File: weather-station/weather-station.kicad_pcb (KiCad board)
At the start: 2 copper layers, 62 x 100 mm, 23 parts, among them P1 CONN_01X05, P2 CONN_01X03, P3 CONN_01X02, P8 CONN_RB, U1 FUELGUAGE, U2 FEATHER, U3 pololu-vreg, U4 adafruit-solar-charger, U5 FEATHER

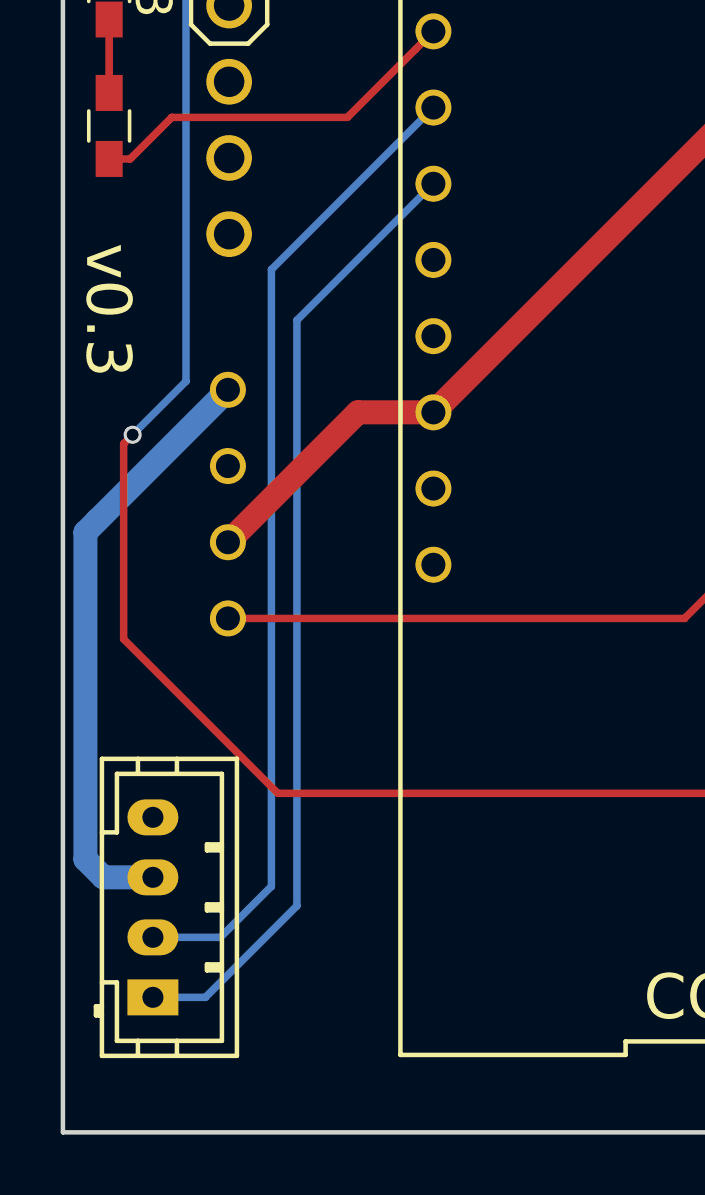
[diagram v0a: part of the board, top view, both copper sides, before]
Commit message: Change RB connector footprint to 2.54mm pitch.
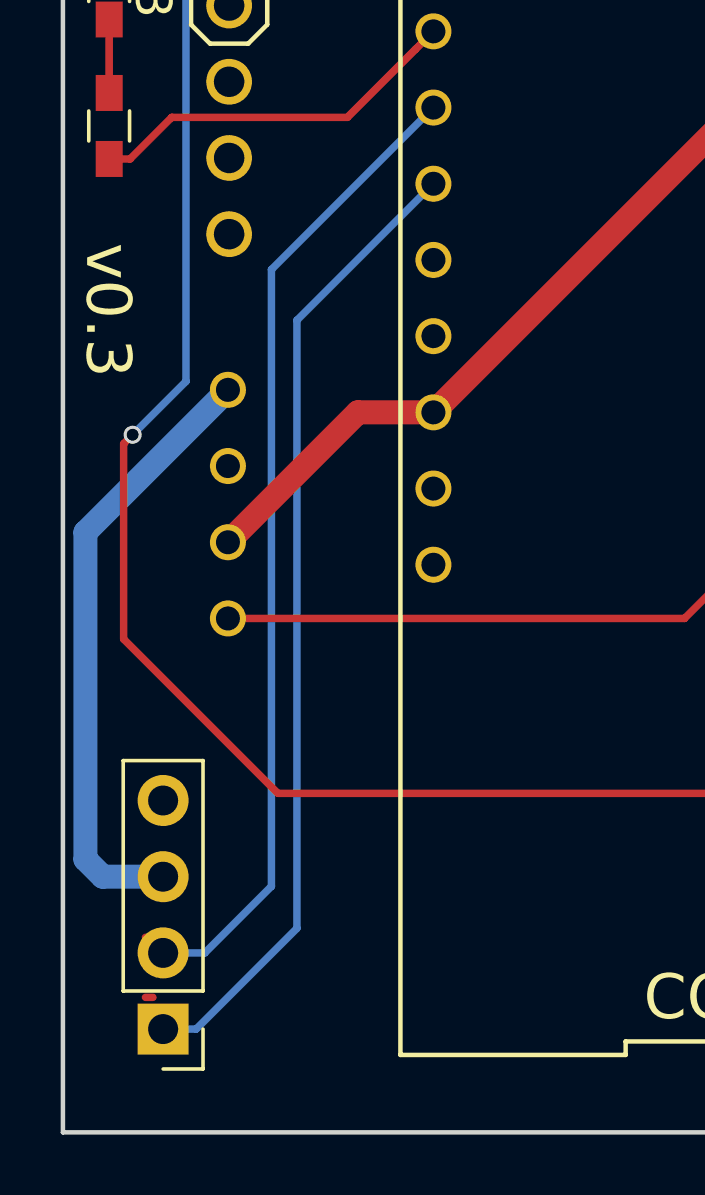
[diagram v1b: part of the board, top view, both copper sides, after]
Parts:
- P8: footprint Connectors_JST:JST_PH_B4B-PH-K_04x2.00mm_Straight -> Socket_Strips:Socket_Strip_Straight_1x04_Pitch2.54mm
- moved P8 1.11 mm to (53.3, 146.6), turned to 180 degrees
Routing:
- net (no net): track 0.00 -> 0.50 mm
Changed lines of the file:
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@@
   (general
     (links 55)
-    (no_connects 0)
+    (no_connects 16)
     (area 49.924999 49.924999 112.075001 150.075001)
     (thickness 1.6)
     (drawings 17)
-    (tracks 192)
+    (tracks 190)
     (zones 0)
     (modules 23)
@@
   )
   (setup
-    (last_trace_width 0.25)
+    (last_trace_width 0.8)
     (user_trace_width 0.203)
     (user_trace_width 0.4)
@@
       (xy -6.476371 1.79874)) (layer B.SilkS) (width 0.01))
   )
-  (module Connectors_JST:JST_PH_B4B-PH-K_04x2.00mm_Straight (layer F.Cu)
-    (at 53 145.5 90)
-    (descr http://www.jst-mfg.com/product/pdf/eng/ePH.pdf)
-    (tags "connector jst ph")
-    (fp_text reference P8 (at -1.5 4 90) (layer F.SilkS) hide
-      (effects (font (size 1 1) (thickness 0.15)))
-    )
-    (fp_text value CONN_RB (at 3 4 90) (layer F.Fab) hide
-      (effects (font (size 1 1) (thickness 0.15)))
-    )
-    (fp_line (start -1.95 2.8) (end -1.95 -1.7) (layer F.SilkS) (width 0.15))
-    (fp_line (start -1.95 -1.7) (end 7.95 -1.7) (layer F.SilkS) (width 0.15))
-    (fp_line (start 7.95 -1.7) (end 7.95 2.8) (layer F.SilkS) (width 0.15))
-    (fp_line (start 7.95 2.8) (end -1.95 2.8) (layer F.SilkS) (width 0.15))
-    (fp_line (start 0.5 -1.7) (end 0.5 -1.2) (layer F.SilkS) (width 0.15))
-    (fp_line (start 0.5 -1.2) (end -1.45 -1.2) (layer F.SilkS) (width 0.15))
-    (fp_line (start -1.45 -1.2) (end -1.45 2.3) (layer F.SilkS) (width 0.15))
-    (fp_line (start -1.45 2.3) (end 7.45 2.3) (layer F.SilkS) (width 0.15))
-    (fp_line (start 7.45 2.3) (end 7.45 -1.2) (layer F.SilkS) (width 0.15))
-    (fp_line (start 7.45 -1.2) (end 5.5 -1.2) (layer F.SilkS) (width 0.15))
-    (fp_line (start 5.5 -1.2) (end 5.5 -1.7) (layer F.SilkS) (width 0.15))
-    (fp_line (start -1.95 -0.5) (end -1.45 -0.5) (layer F.SilkS) (width 0.15))
-    (fp_line (start -1.95 0.8) (end -1.45 0.8) (layer F.SilkS) (width 0.15))
-    (fp_line (start 7.45 -0.5) (end 7.95 -0.5) (layer F.SilkS) (width 0.15))
-    (fp_line (start 7.45 0.8) (end 7.95 0.8) (layer F.SilkS) (width 0.15))
-    (fp_line (start -0.3 -1.7) (end -0.3 -1.9) (layer F.SilkS) (width 0.15))
-    (fp_line (start -0.3 -1.9) (end -0.6 -1.9) (layer F.SilkS) (width 0.15))
-    (fp_line (start -0.6 -1.9) (end -0.6 -1.7) (layer F.SilkS) (width 0.15))
-    (fp_line (start -0.3 -1.8) (end -0.6 -1.8) (layer F.SilkS) (width 0.15))
-    (fp_line (start 0.9 2.3) (end 0.9 1.8) (layer F.SilkS) (width 0.15))
-    (fp_line (start 0.9 1.8) (end 1.1 1.8) (layer F.SilkS) (width 0.15))
-    (fp_line (start 1.1 1.8) (end 1.1 2.3) (layer F.SilkS) (width 0.15))
-    (fp_line (start 1 2.3) (end 1 1.8) (layer F.SilkS) (width 0.15))
-    (fp_line (start 2.9 2.3) (end 2.9 1.8) (layer F.SilkS) (width 0.15))
-    (fp_line (start 2.9 1.8) (end 3.1 1.8) (layer F.SilkS) (width 0.15))
-    (fp_line (start 3.1 1.8) (end 3.1 2.3) (layer F.SilkS) (width 0.15))
-    (fp_line (start 3 2.3) (end 3 1.8) (layer F.SilkS) (width 0.15))
-    (fp_line (start 4.9 2.3) (end 4.9 1.8) (layer F.SilkS) (width 0.15))
-    (fp_line (start 4.9 1.8) (end 5.1 1.8) (layer F.SilkS) (width 0.15))
-    (fp_line (start 5.1 1.8) (end 5.1 2.3) (layer F.SilkS) (width 0.15))
-    (fp_line (start 5 2.3) (end 5 1.8) (layer F.SilkS) (width 0.15))
-    (fp_line (start -2.45 3.3) (end -2.45 -2.2) (layer F.CrtYd) (width 0.05))
-    (fp_line (start -2.45 -2.2) (end 8.45 -2.2) (layer F.CrtYd) (width 0.05))
-    (fp_line (start 8.45 -2.2) (end 8.45 3.3) (layer F.CrtYd) (width 0.05))
-    (fp_line (start 8.45 3.3) (end -2.45 3.3) (layer F.CrtYd) (width 0.05))
-    (pad 1 thru_hole rect (at 0 0 90) (size 1.2 1.7) (drill 0.7) (layers *.Cu *.Mask)
-      (net 10 /RB_RX))
-    (pad 2 thru_hole oval (at 2 0 90) (size 1.2 1.7) (drill 0.7) (layers *.Cu *.Mask)
-      (net 11 /RB_TX))
-    (pad 3 thru_hole oval (at 4 0 90) (size 1.2 1.7) (drill 0.7) (layers *.Cu *.Mask)
-      (net 5 +5V))
-    (pad 4 thru_hole oval (at 6 0 90) (size 1.2 1.7) (drill 0.7) (layers *.Cu *.Mask)
-      (net 3 GND))
-  )
   (module conservify:feather (layer F.Cu)
     (at 72.51 122.19 90)
@@
     )
   )
+  (module Socket_Strips:Socket_Strip_Straight_1x04_Pitch2.54mm (layer F.Cu)
+    (at 53.34 146.558 180)
+    (descr "Through hole straight socket strip, 1x04, 2.54mm pitch, single row")
+    (tags "Through hole socket strip THT 1x04 2.54mm single row")
+    (fp_text reference P8 (at 0 -2.33 180) (layer F.SilkS) hide
+      (effects (font (size 1 1) (thickness 0.15)))
+    )
+    (fp_text value CONN_RB (at 0 9.95 180) (layer F.Fab)
+      (effects (font (size 1 1) (thickness 0.15)))
+    )
+    (fp_line (start -1.27 -1.27) (end -1.27 8.89) (layer F.Fab) (width 0.1))
+    (fp_line (start -1.27 8.89) (end 1.27 8.89) (layer F.Fab) (width 0.1))
+    (fp_line (start 1.27 8.89) (end 1.27 -1.27) (layer F.Fab) (width 0.1))
+    (fp_line (start 1.27 -1.27) (end -1.27 -1.27) (layer F.Fab) (width 0.1))
+    (fp_line (start -1.33 1.27) (end -1.33 8.95) (layer F.SilkS) (width 0.12))
+    (fp_line (start -1.33 8.95) (end 1.33 8.95) (layer F.SilkS) (width 0.12))
+    (fp_line (start 1.33 8.95) (end 1.33 1.27) (layer F.SilkS) (width 0.12))
+    (fp_line (start 1.33 1.27) (end -1.33 1.27) (layer F.SilkS) (width 0.12))
+    (fp_line (start -1.33 0) (end -1.33 -1.33) (layer F.SilkS) (width 0.12))
+    (fp_line (start -1.33 -1.33) (end 0 -1.33) (layer F.SilkS) (width 0.12))
+    (fp_line (start -1.8 -1.8) (end -1.8 9.4) (layer F.CrtYd) (width 0.05))
+    (fp_line (start -1.8 9.4) (end 1.8 9.4) (layer F.CrtYd) (width 0.05))
+    (fp_line (start 1.8 9.4) (end 1.8 -1.8) (layer F.CrtYd) (width 0.05))
+    (fp_line (start 1.8 -1.8) (end -1.8 -1.8) (layer F.CrtYd) (width 0.05))
+    (fp_text user %R (at 0 -2.33 180) (layer F.Fab)
+      (effects (font (size 1 1) (thickness 0.15)))
+    )
+    (pad 1 thru_hole rect (at 0 0 180) (size 1.7 1.7) (drill 1) (layers *.Cu *.Mask)
+      (net 10 /RB_RX))
+    (pad 2 thru_hole oval (at 0 2.54 180) (size 1.7 1.7) (drill 1) (layers *.Cu *.Mask)
+      (net 11 /RB_TX))
+    (pad 3 thru_hole oval (at 0 5.08 180) (size 1.7 1.7) (drill 1) (layers *.Cu *.Mask)
+      (net 5 +5V))
+    (pad 4 thru_hole oval (at 0 7.62 180) (size 1.7 1.7) (drill 1) (layers *.Cu *.Mask)
+      (net 3 GND))
+    (model ${KISYS3DMOD}/Socket_Strips.3dshapes/Socket_Strip_Straight_1x04_Pitch2.54mm.wrl
+      (at (xyz 0 -0.15 0))
+      (scale (xyz 1 1 1))
+      (rotate (xyz 0 0 270))
+    )
+  )
   (gr_text D3 (at 53 111.7 270) (layer F.SilkS)
     (effects (font (size 1.2 1.2) (thickness 0.2)))
@@
   (gr_line (start 50 150) (end 112 150) (angle 90) (layer Edge.Cuts) (width 0.15))
   (gr_line (start 50 50) (end 50 150) (angle 90) (layer Edge.Cuts) (width 0.15))
+  (segment (start 53 143.5) (end 52.75 143.5) (width 0.25) (layer F.Cu) (net 0))
+  (segment (start 53 145.5) (end 52.75 145.5) (width 0.25) (layer F.Cu) (net 0))
   (segment (start 54.54 62.38) (end 54.54 58.06) (width 0.8) (layer F.Cu) (net 1))
   (segment (start 54.54 58.06) (end 58.1 54.5) (width 0.8) (layer F.Cu) (net 1))
@@
   (segment (start 85.75 122.92) (end 85.75 103.861998) (width 0.8) (layer B.Cu) (net 4))
   (segment (start 88.84 126.01) (end 85.75 122.92) (width 0.8) (layer B.Cu) (net 4))
-  (segment (start 50.75 140.9) (end 50.75 130) (width 0.8) (layer B.Cu) (net 5))
-  (segment (start 50.75 130) (end 51.14999 129.60001) (width 0.8) (layer B.Cu) (net 5))
-  (segment (start 53 141.5) (end 51.35 141.5) (width 0.8) (layer B.Cu) (net 5))
-  (segment (start 51.35 141.5) (end 50.75 140.9) (width 0.8) (layer B.Cu) (net 5))
-  (segment (start 51.14999 129.60001) (end 55.5 125.25) (width 0.8) (layer B.Cu) (net 5))
+  (segment (start 55.5 125.25) (end 50.75 130) (width 0.8) (layer B.Cu) (net 5))
+  (segment (start 50.75 130) (end 50.75 140.9) (width 0.8) (layer B.Cu) (net 5))
+  (segment (start 50.75 140.9) (end 51.328 141.478) (width 0.8) (layer B.Cu) (net 5))
+  (segment (start 51.328 141.478) (end 53.34 141.478) (width 0.8) (layer B.Cu) (net 5))
   (segment (start 62.35 103.14) (end 62.35 67.4976) (width 0.25) (layer F.Cu) (net 6))
   (segment (start 62.35 67.4976) (end 59.7724 64.92) (width 0.25) (layer F.Cu) (net 6))
@@
   (segment (start 86.549999 128.189999) (end 87.514999 127.224999) (width 0.25) (layer F.Cu) (net 9))
   (segment (start 88.84 128.55) (end 87.514999 127.224999) (width 0.25) (layer F.Cu) (net 9))
-  (segment (start 62.35 118.38) (end 57.799999 122.930001) (width 0.25) (layer B.Cu) (net 10))
-  (segment (start 57.799999 122.930001) (end 57.799999 142.450001) (width 0.25) (layer B.Cu) (net 10))
-  (segment (start 57.799999 142.450001) (end 54.75 145.5) (width 0.25) (layer B.Cu) (net 10))
-  (segment (start 54.75 145.5) (end 53 145.5) (width 0.25) (layer B.Cu) (net 10))
-  (segment (start 53.25 145.5) (end 53 145.5) (width 0.25) (layer B.Cu) (net 10))
-  (segment (start 53 145.5) (end 52.75 145.5) (width 0.25) (layer F.Cu) (net 10))
-  (segment (start 53 143.5) (end 55.25 143.5) (width 0.25) (layer B.Cu) (net 11))
-  (segment (start 55.25 143.5) (end 56.949988 141.800012) (width 0.25) (layer B.Cu) (net 11))
+  (segment (start 53.34 146.558) (end 54.44 146.558) (width 0.25) (layer B.Cu) (net 10))
+  (segment (start 54.44 146.558) (end 57.799999 143.198001) (width 0.25) (layer B.Cu) (net 10))
+  (segment (start 57.799999 143.198001) (end 57.799999 122.930001) (width 0.25) (layer B.Cu) (net 10))
+  (segment (start 57.799999 122.930001) (end 62.35 118.38) (width 0.25) (layer B.Cu) (net 10))
+  (segment (start 53.34 144.018) (end 54.732 144.018) (width 0.25) (layer B.Cu) (net 11))
+  (segment (start 54.732 144.018) (end 56.949988 141.800012) (width 0.25) (layer B.Cu) (net 11))
   (segment (start 56.949988 121.240012) (end 56.949988 141.800012) (width 0.25) (layer B.Cu) (net 11))
-  (segment (start 53 143.5) (end 52.75 143.5) (width 0.25) (layer F.Cu) (net 11))
   (segment (start 62.35 115.84) (end 56.949988 121.240012) (width 0.25) (layer B.Cu) (net 11))
   (segment (start 99.625011 129.75) (end 99.625011 109.976004) (width 0.25) (layer B.Cu) (net 12))
